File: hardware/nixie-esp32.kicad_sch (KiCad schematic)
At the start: 21 parts, among them J1 USB4216-03-A_REVA, SW1 RESET, SW2 BOOT, U1 AP7361C-33E-13, U2 ESP32-S3-WROOM-1

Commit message: WIP SN74141 redesign
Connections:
- net ESP32_GPIO17: now reaches U2.10 (GPIO17/U1TXD/ADC2_CH6)
- net ESP32_GPIO18: now reaches U2.11 (GPIO18/U1RXD/ADC2_CH7/CLK_OUT3)
- net ESP32_GPIO12: now reaches U2.20 (GPIO12/TOUCH12/ADC2_CH1/FSPICLK/FSPIIO6/SUBSPICLK)
- net ESP32_GPIO13: now reaches U2.21 (GPIO13/TOUCH13/ADC2_CH2/FSPIQ/FSPIIO7/SUBSPIQ)
- net ESP32_GPIO14: now reaches U2.22 (GPIO14/TOUCH14/ADC2_CH3/FSPIWP/FSPIDQS/SUBSPIWP)
- net ESP32_GPIO21: now reaches U2.23 (GPIO21)
- net ESP32_GPIO38: now reaches U2.31 (GPIO38/FSPIWP/SUBSPIWP)
- net ESP32_GPIO2: now reaches U2.38 (GPIO2/TOUCH2/ADC1_CH1)
- net ESP32_GPIO1: now reaches U2.39 (GPIO1/TOUCH1/ADC1_CH0)
- net ESP32_GPIO5: now reaches U2.5 (GPIO5/TOUCH5/ADC1_CH4)
- net ESP32_GPIO6: now reaches U2.6 (GPIO6/TOUCH6/ADC1_CH5)
- net ESP32_GPIO7: now reaches U2.7 (GPIO7/TOUCH7/ADC1_CH6)
- no-connect marks 32 -> 20
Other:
- sheet Nixies ports: added none; removed HV_BLANK, HV_CLOCK, HV_DATA, HV_LATCH

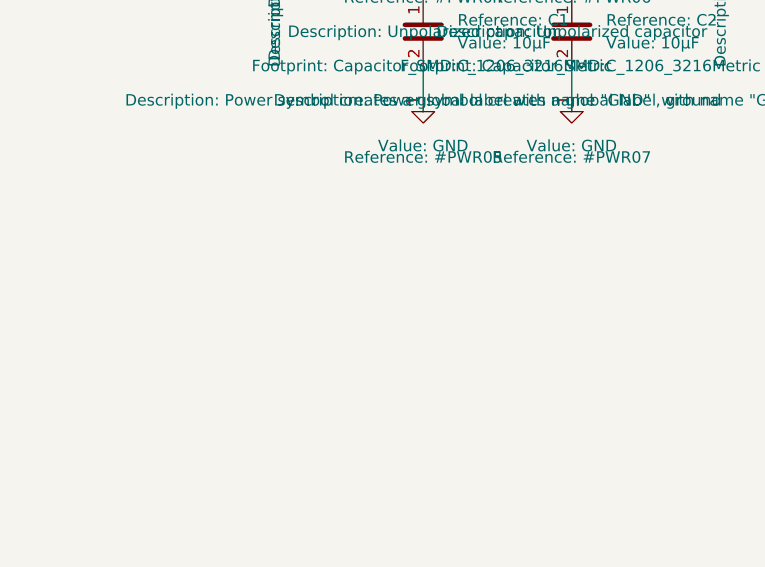
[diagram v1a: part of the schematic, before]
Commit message: Add 5V and 170V status LED indicators
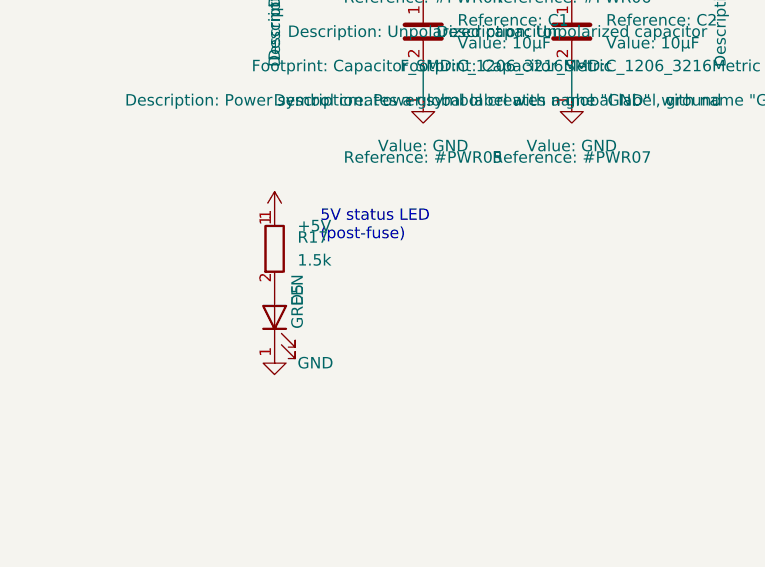
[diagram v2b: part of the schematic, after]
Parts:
- added D5: GREEN, LED_SMD:LED_0805_2012Metric, symbol Device:LED
- added R17: 1.5k, Resistor_SMD:R_0805_2012Metric, symbol Device:R
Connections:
- net +5V: now also R17.1
- net GND: now also D5.1 (K)
- new net: D5.2 (A), R17.2
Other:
- note added: "5V status LED (post-fuse)"
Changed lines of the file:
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@@
     )
   )
-  (sheet_instances
+  	(symbol
+		(lib_id "power:+5V")
+		(at 35.56 160.02 0)
+		(unit 1)
+		(exclude_from_sim no)
+		(in_bom yes)
+		(on_board yes)
+		(dnp no)
+		(property "Reference" "#PWR069" (at 38.1 158.75 0) (effects (font (size 1.27 1.27)) (justify left) (hide yes)))
+		(property "Value" "+5V" (at 38.1 161.29000000000002 0) (effects (font (size 1.27 1.27)) (justify left)))
+		(property "Footprint" "" (at 35.56 160.02 0) (effects (font (size 1.27 1.27)) (hide yes)))
+		(property "Datasheet" "" (at 35.56 160.02 0) (effects (font (size 1.27 1.27)) (hide yes)))
+		(pin "1")
+		(instances (project "nixie-esp32" (path "/54b4b31b-75dd-48a2-8c91-a3f3099728fc" (reference "#PWR069") (unit 1))))
+	)
+	(symbol
+		(lib_id "Device:R")
+		(at 35.56 163.83 0)
+		(unit 1)
+		(exclude_from_sim no)
+		(in_bom yes)
+		(on_board yes)
+		(dnp no)
+		(property "Reference" "R17" (at 38.1 162.56 0) (effects (font (size 1.27 1.27)) (justify left)))
+		(property "Value" "1.5k" (at 38.1 165.10000000000002 0) (effects (font (size 1.27 1.27)) (justify left)))
+		(property "Footprint" "Resistor_SMD:R_0805_2012Metric" (at 35.56 163.83 0) (effects (font (size 1.27 1.27)) (hide yes)))
+		(property "Datasheet" "" (at 35.56 163.83 0) (effects (font (size 1.27 1.27)) (hide yes)))
+		(pin "1")
+		(pin "2")
+		(instances (project "nixie-esp32" (path "/54b4b31b-75dd-48a2-8c91-a3f3099728fc" (reference "R17") (unit 1))))
+	)
+	(symbol
+		(lib_id "Device:LED")
+		(at 35.56 171.45 90)
+		(unit 1)
+		(exclude_from_sim no)
+		(in_bom yes)
+		(on_board yes)
+		(dnp no)
+		(property "Reference" "D5" (at 38.1 170.17999999999998 0) (effects (font (size 1.27 1.27)) (justify left)))
+		(property "Value" "GREEN" (at 38.1 172.72 0) (effects (font (size 1.27 1.27)) (justify left)))
+		(property "Footprint" "LED_SMD:LED_0805_2012Metric" (at 35.56 171.45 0) (effects (font (size 1.27 1.27)) (hide yes)))
+		(property "Datasheet" "" (at 35.56 171.45 0) (effects (font (size 1.27 1.27)) (hide yes)))
+		(pin "1")
+		(pin "2")
+		(instances (project "nixie-esp32" (path "/54b4b31b-75dd-48a2-8c91-a3f3099728fc" (reference "D5") (unit 1))))
+	)
+	(symbol
+		(lib_id "power:GND")
+		(at 35.56 175.26 0)
+		(unit 1)
+		(exclude_from_sim no)
+		(in_bom yes)
+		(on_board yes)
+		(dnp no)
+		(property "Reference" "#PWR070" (at 38.1 173.98999999999998 0) (effects (font (size 1.27 1.27)) (justify left) (hide yes)))
+		(property "Value" "GND" (at 38.1 176.53 0) (effects (font (size 1.27 1.27)) (justify left)))
+		(property "Footprint" "" (at 35.56 175.26 0) (effects (font (size 1.27 1.27)) (hide yes)))
+		(property "Datasheet" "" (at 35.56 175.26 0) (effects (font (size 1.27 1.27)) (hide yes)))
+		(pin "1")
+		(instances (project "nixie-esp32" (path "/54b4b31b-75dd-48a2-8c91-a3f3099728fc" (reference "#PWR070") (unit 1))))
+	)
+	(text "5V status LED\n(post-fuse)" (at 40.64 161.29 0) (effects (font (size 1.27 1.27)) (justify left)))
+(sheet_instances
     (path "/" (page "1"))
   )
